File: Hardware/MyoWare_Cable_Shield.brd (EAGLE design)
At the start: 52.3 x 20.7 mm, 18 parts

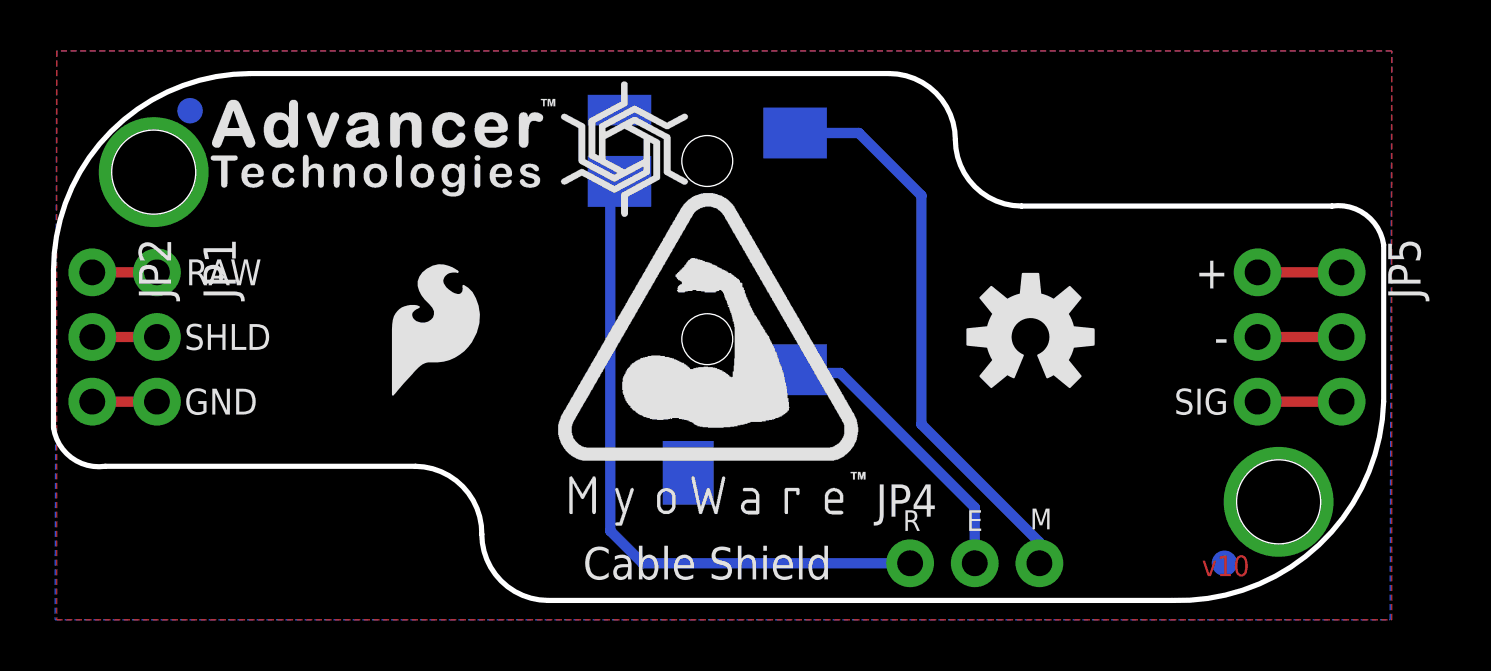
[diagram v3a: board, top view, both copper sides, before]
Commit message: scooted the fiducials inward just a bit for better recognition
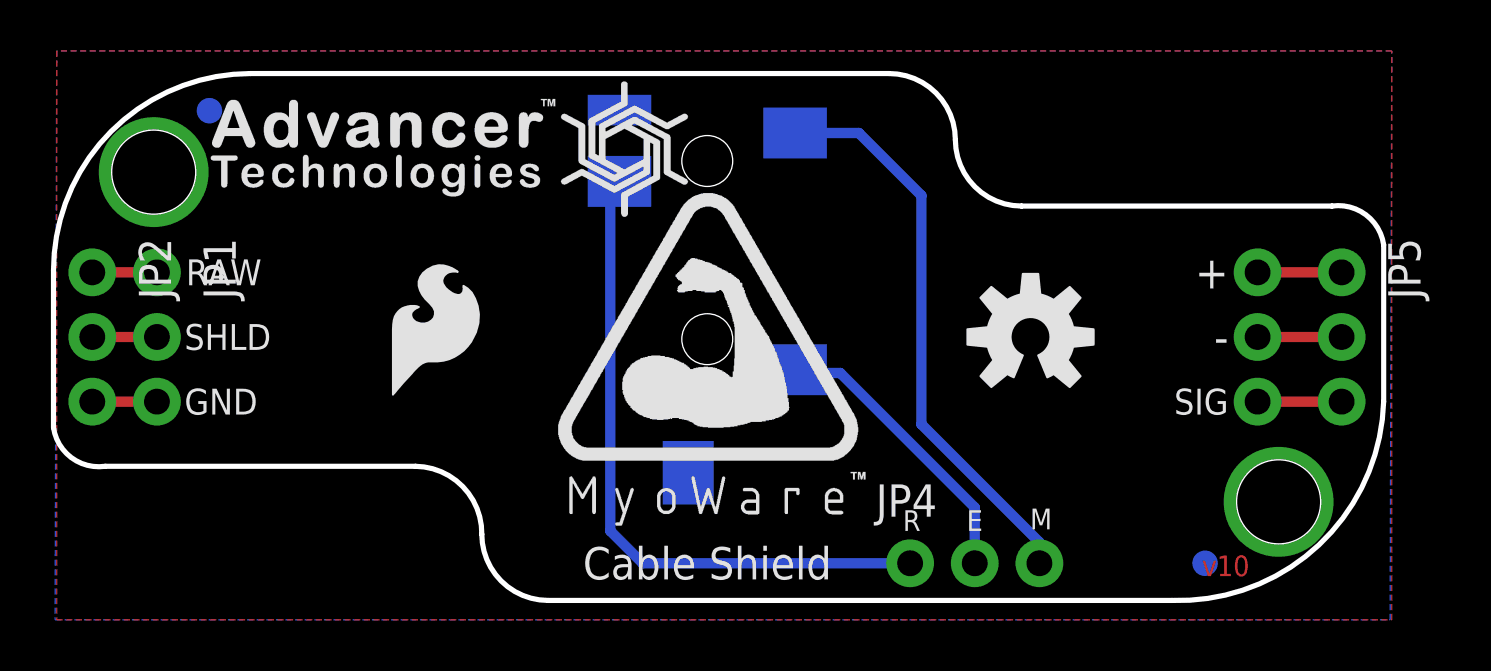
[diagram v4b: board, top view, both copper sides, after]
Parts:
- moved FID1 0.76 mm to (19.6, -8.89)
- moved FID2 0.76 mm to (-19.6, 8.89)
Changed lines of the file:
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@@
 <setting verticaltext="up"/>
 </settings>
-<grid distance="0.05" unitdist="inch" unit="inch" style="lines" multiple="1" display="yes" altdistance="0.005" altunitdist="inch" altunit="inch"/>
+<grid distance="0.01" unitdist="inch" unit="inch" style="lines" multiple="1" display="yes" altdistance="0.001" altunitdist="inch" altunit="inch"/>
 <layers>
 <layer number="1" name="Top" color="4" fill="1" visible="yes" active="yes"/>
@@
 <layer number="18" name="Vias" color="2" fill="1" visible="yes" active="yes"/>
 <layer number="19" name="Unrouted" color="6" fill="1" visible="yes" active="yes"/>
-<layer number="20" name="Dimension" color="15" fill="1" visible="yes" active="yes"/>
-<layer number="21" name="tPlace" color="16" fill="1" visible="yes" active="yes"/>
-<layer number="22" name="bPlace" color="14" fill="1" visible="yes" active="yes"/>
+<layer number="20" name="Dimension" color="6" fill="1" visible="yes" active="yes"/>
+<layer number="21" name="tPlace" color="6" fill="1" visible="yes" active="yes"/>
+<layer number="22" name="bPlace" color="6" fill="1" visible="yes" active="yes"/>
 <layer number="23" name="tOrigins" color="15" fill="1" visible="yes" active="yes"/>
 <layer number="24" name="bOrigins" color="15" fill="1" visible="yes" active="yes"/>
@@
 <element name="STANDOFF1" library="SparkFun-Electromechanical" package="STAND-OFF" value="STAND-OFF" x="-21.74875" y="6.477"/>
 <element name="STANDOFF2" library="SparkFun-Electromechanical" package="STAND-OFF" value="STAND-OFF" x="22.44725" y="-6.477"/>
-<element name="FID2" library="SparkFun-Aesthetics" package="FIDUCIAL-1X2" value="FIDUCIAL1X2" x="-20.32" y="8.89" rot="MR0"/>
-<element name="FID1" library="SparkFun-Aesthetics" package="FIDUCIAL-1X2" value="FIDUCIAL1X2" x="20.32" y="-8.89" rot="MR0"/>
+<element name="FID2" library="SparkFun-Aesthetics" package="FIDUCIAL-1X2" value="FIDUCIAL1X2" x="-19.558" y="8.89" rot="MR0"/>
+<element name="FID1" library="SparkFun-Aesthetics" package="FIDUCIAL-1X2" value="FIDUCIAL1X2" x="19.558" y="-8.89" rot="MR0"/>
 <element name="JP3" library="SparkFun-Connectors" package="AUDIO-JACK-3.5MM-SMD" value="3.5mm Jack" x="0" y="10.414" rot="MR270">
 <attribute name="PROD_ID" value="CONN-10353" x="0" y="10.414" size="1.778" layer="28" rot="MR270" display="off"/>
